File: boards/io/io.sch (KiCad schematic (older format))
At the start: 98 parts, among them J1 CU, J2 KB_ROW, J3 KB_COL, U1 74ACT32, U2 74ACT08, U3 74ACT00, U4 AT28C256-PLCC32, U5 62256-TSOP, U6 RC1602A, U7 74AC273, U8 74ACT244

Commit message: Part names
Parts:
- J1: value CU -> 61304021021
- R1: value 1 -> 0
- RV1: value 10-20k -> BOURNS 3296Y-1-203LF
- U1: value 74ACT32 -> SN74ACT32PWR
- U2: value 74ACT08 -> SN74ACT08PWR
- U3: value 74ACT00 -> 74ACT00MTCX
- U5: value 62256-TSOP -> CY62256NLL-55ZXI
- U6: value RC1602A -> SSW-116-01-T-S
- U7: value 74AC273 -> MC74AC273DTR2G
- U8: value 74ACT244 -> SN74ACT244PW
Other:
- moved on the sheet: C3, U2E, U3E
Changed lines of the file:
@@
 P 7550 2150
 F 0 "U5" H 8100 1200 50  0000 C CNN
-F 1 "62256-TSOP" H 7950 1050 50  0000 C CNN
+F 1 "CY62256NLL-55ZXI" H 7950 1050 50  0000 C CNN
 F 2 "Package_SO:TSOP-I-28_11.8x8mm_P0.55mm" H 7550 3000 50  0001 C CNN
 F 3 "http://www.farnell.com/datasheets/1674430.pdf" H 7550 3000 50  0001 C CNN
@@
 AR Path="/5E594F4F" Ref="U6"  Part="1"
 F 0 "U6" H 10650 1350 50  0000 C CNN
-F 1 "RC1602A" H 10850 1500 50  0000 C CNN
+F 1 "SSW-116-01-T-S" H 10850 1500 50  0000 C CNN
 F 2 "Connector_PinSocket_2.54mm:PinSocket_1x16_P2.54mm_Vertical" H 10450 1250 50  0001 C CNN
 F 3 "http://www.raystar-optronics.com/down.php?ProID=18" H 10450 1950 50  0001 C CNN
@@
 P 4850 4150
 F 0 "U2" H 4850 4475 50  0000 C CNN
-F 1 "74ACT08" H 4850 4384 50  0000 C CNN
+F 1 "SN74ACT08PWR" H 4850 4384 50  0000 C CNN
 F 2 "Package_SO:TSSOP-14_4.4x5mm_P0.65mm" H 4850 4150 50  0001 C CNN
 F 3 "http://www.ti.com/lit/gpn/sn74LS08" H 4850 4150 50  0001 C CNN
@@
 P 4850 4750
 F 0 "U2" H 4850 5075 50  0000 C CNN
-F 1 "74ACT08" H 4850 4984 50  0000 C CNN
+F 1 "SN74ACT08PWR" H 4850 4984 50  0000 C CNN
 F 2 "Package_SO:TSSOP-14_4.4x5mm_P0.65mm" H 4850 4750 50  0001 C CNN
 F 3 "http://www.ti.com/lit/gpn/sn74LS08" H 4850 4750 50  0001 C CNN
@@
 P 4300 6500
 F 0 "U2" H 4300 6825 50  0000 C CNN
-F 1 "74ACT08" H 4300 6734 50  0000 C CNN
+F 1 "SN74ACT08PWR" H 4300 6734 50  0000 C CNN
 F 2 "Package_SO:TSSOP-14_4.4x5mm_P0.65mm" H 4300 6500 50  0001 C CNN
 F 3 "http://www.ti.com/lit/gpn/sn74LS08" H 4300 6500 50  0001 C CNN
@@
 P 9000 4550
 F 0 "U2" H 9000 4875 50  0000 C CNN
-F 1 "74ACT08" H 9000 4784 50  0000 C CNN
+F 1 "SN74ACT08PWR" H 9000 4784 50  0000 C CNN
 F 2 "Package_SO:TSSOP-14_4.4x5mm_P0.65mm" H 9000 4550 50  0001 C CNN
 F 3 "http://www.ti.com/lit/gpn/sn74LS08" H 9000 4550 50  0001 C CNN
@@
 P 5550 4450
 F 0 "U3" H 5550 4775 50  0000 C CNN
-F 1 "74ACT00" H 5550 4684 50  0000 C CNN
+F 1 "74ACT00MTCX" H 5550 4684 50  0000 C CNN
 F 2 "Package_SO:TSSOP-14_4.4x5mm_P0.65mm" H 5550 4450 50  0001 C CNN
 F 3 "http://www.ti.com/lit/gpn/sn74hc00" H 5550 4450 50  0001 C CNN
@@
 P 6150 4700
 F 0 "U3" H 6150 5025 50  0000 C CNN
-F 1 "74ACT00" H 6150 4934 50  0000 C CNN
+F 1 "74ACT00MTCX" H 6150 4934 50  0000 C CNN
 F 2 "Package_SO:TSSOP-14_4.4x5mm_P0.65mm" H 6150 4700 50  0001 C CNN
 F 3 "http://www.ti.com/lit/gpn/sn74hc00" H 6150 4700 50  0001 C CNN
@@
 P 8400 4250
 F 0 "U3" H 8400 4575 50  0000 C CNN
-F 1 "74ACT00" H 8400 4484 50  0000 C CNN
+F 1 "74ACT00MTCX" H 8400 4484 50  0000 C CNN
 F 2 "Package_SO:TSSOP-14_4.4x5mm_P0.65mm" H 8400 4250 50  0001 C CNN
 F 3 "http://www.ti.com/lit/gpn/sn74hc00" H 8400 4250 50  0001 C CNN
@@
 P 7600 4250
 F 0 "U1" H 7600 4575 50  0000 C CNN
-F 1 "74ACT32" H 7600 4484 50  0000 C CNN
+F 1 "SN74ACT32PWR" H 7600 4484 50  0000 C CNN
 F 2 "Package_SO:TSSOP-14_4.4x5mm_P0.65mm" H 7600 4250 50  0001 C CNN
 F 3 "http://www.ti.com/lit/gpn/sn74LS32" H 7600 4250 50  0001 C CNN
@@
 P 6250 5600
 F 0 "U1" H 6250 5925 50  0000 C CNN
-F 1 "74ACT32" H 6250 5834 50  0000 C CNN
+F 1 "SN74ACT32PWR" H 6250 5834 50  0000 C CNN
 F 2 "Package_SO:TSSOP-14_4.4x5mm_P0.65mm" H 6250 5600 50  0001 C CNN
 F 3 "http://www.ti.com/lit/gpn/sn74LS32" H 6250 5600 50  0001 C CNN
@@
 P 3450 9150
 F 0 "U1" H 3680 9196 50  0000 L CNN
-F 1 "74ACT32" H 3680 9105 50  0000 L CNN
+F 1 "SN74ACT32PWR" H 3680 9105 50  0000 L CNN
 F 2 "Package_SO:TSSOP-14_4.4x5mm_P0.65mm" H 3450 9150 50  0001 C CNN
 F 3 "http://www.ti.com/lit/gpn/sn74LS32" H 3450 9150 50  0001 C CNN
@@
 L 74xx:74HC00 U3
 U 5 1 5E65CA62
-P 4400 9150
-F 0 "U3" H 4630 9196 50  0000 L CNN
-F 1 "74ACT00" H 4630 9105 50  0000 L CNN
-F 2 "Package_SO:TSSOP-14_4.4x5mm_P0.65mm" H 4400 9150 50  0001 C CNN
-F 3 "http://www.ti.com/lit/gpn/sn74hc00" H 4400 9150 50  0001 C CNN
-	5    4400 9150
+P 4550 9150
+F 0 "U3" H 4780 9196 50  0000 L CNN
+F 1 "74ACT00MTCX" H 4780 9105 50  0000 L CNN
+F 2 "Package_SO:TSSOP-14_4.4x5mm_P0.65mm" H 4550 9150 50  0001 C CNN
+F 3 "http://www.ti.com/lit/gpn/sn74hc00" H 4550 9150 50  0001 C CNN
+	5    4550 9150
 	1    0    0    -1
 $EndComp
@@
 L 74xx:74LS08 U2
 U 5 1 5E65F2AF
-P 5250 9150
-F 0 "U2" H 5480 9196 50  0000 L CNN
-F 1 "74ACT08" H 5480 9105 50  0000 L CNN
-F 2 "Package_SO:TSSOP-14_4.4x5mm_P0.65mm" H 5250 9150 50  0001 C CNN
-F 3 "http://www.ti.com/lit/gpn/sn74LS08" H 5250 9150 50  0001 C CNN
-	5    5250 9150
+P 5650 9150
+F 0 "U2" H 5880 9196 50  0000 L CNN
+F 1 "SN74ACT08PWR" H 5880 9105 50  0000 L CNN
+F 2 "Package_SO:TSSOP-14_4.4x5mm_P0.65mm" H 5650 9150 50  0001 C CNN
+F 3 "http://www.ti.com/lit/gpn/sn74LS08" H 5650 9150 50  0001 C CNN
+	5    5650 9150
 	1    0    0    -1
 $EndComp
@@
 P 10550 4700
 F 0 "U7" H 10950 4150 50  0000 C CNN
-F 1 "74AC273" H 10950 4000 50  0000 C CNN
+F 1 "MC74AC273DTR2G" H 10950 4000 50  0000 C CNN
 F 2 "Package_SO:TSSOP-20_4.4x6.5mm_P0.65mm" H 10550 4700 50  0001 C CNN
 F 3 "https://assets.nexperia.com/documents/data-sheet/74HC_HCT273.pdf" H 10550 4700 50  0001 C CNN
@@
 P 14250 4700
 F 0 "U8" H 14650 4150 50  0000 C CNN
-F 1 "74ACT244" H 14600 4000 50  0000 C CNN
+F 1 "SN74ACT244PW" H 14600 4000 50  0000 C CNN
 F 2 "Package_SO:TSSOP-20_4.4x6.5mm_P0.65mm" H 14250 4700 50  0001 C CNN
 F 3 "https://assets.nexperia.com/documents/data-sheet/74HC_HCT244.pdf" H 14250 4700 50  0001 C CNN
@@
 P 7650 5300
 F 0 "U1" H 7650 5625 50  0000 C CNN
-F 1 "74ACT32" H 7650 5534 50  0000 C CNN
+F 1 "SN74ACT32PWR" H 7650 5534 50  0000 C CNN
 F 2 "Package_SO:TSSOP-14_4.4x5mm_P0.65mm" H 7650 5300 50  0001 C CNN
 F 3 "http://www.ti.com/lit/gpn/sn74LS32" H 7650 5300 50  0001 C CNN
@@
 P 7650 5850
 F 0 "U1" H 7650 6175 50  0000 C CNN
-F 1 "74ACT32" H 7650 6084 50  0000 C CNN
+F 1 "SN74ACT32PWR" H 7650 6084 50  0000 C CNN
 F 2 "Package_SO:TSSOP-14_4.4x5mm_P0.65mm" H 7650 5850 50  0001 C CNN
 F 3 "http://www.ti.com/lit/gpn/sn74LS32" H 7650 5850 50  0001 C CNN
@@
 P 4300 7050
 F 0 "U3" H 4300 7375 50  0000 C CNN
-F 1 "74ACT00" H 4300 7284 50  0000 C CNN
+F 1 "74ACT00MTCX" H 4300 7284 50  0000 C CNN
 F 2 "Package_SO:TSSOP-14_4.4x5mm_P0.65mm" H 4300 7050 50  0001 C CNN
 F 3 "http://www.ti.com/lit/gpn/sn74hc00" H 4300 7050 50  0001 C CNN
@@
 P 11300 1850
 F 0 "RV1" H 11230 1804 50  0000 R CNN
-F 1 "10-20k" H 11230 1895 50  0000 R CNN
+F 1 "BOURNS 3296Y-1-203LF" H 11230 1895 50  0000 R CNN
 F 2 "Potentiometer_THT:Potentiometer_Bourns_3296Z_Horizontal" H 11300 1850 50  0001 C CNN
 F 3 "~" H 11300 1850 50  0001 C CNN
@@
 P 11100 2350
 F 0 "R1" V 11200 2350 50  0000 C CNN
-F 1 "1" V 11000 2350 50  0000 C CNN
+F 1 "0" V 11000 2350 50  0000 C CNN
 F 2 "Resistor_SMD:R_0805_2012Metric" V 11030 2350 50  0001 C CNN
 F 3 "~" H 11100 2350 50  0001 C CNN
@@
 AR Path="/5E72DAA8" Ref="J1"  Part="1"
 F 0 "J1" H 1800 4217 50  0000 C CNN
-F 1 "CU" H 1800 4126 50  0000 C CNN
+F 1 "61304021021" H 1800 4126 50  0000 C CNN
 F 2 "Connector_PinHeader_2.54mm:PinHeader_2x20_P2.54mm_Horizontal" H 1750 3100 50  0001 C CNN
 F 3 "~" H 1750 3100 50  0001 C CNN
@@
 L power:GND #PWR0102
 U 1 1 5E7372E2
-P 4400 9650
-F 0 "#PWR0102" H 4400 9400 50  0001 C CNN
-F 1 "GND" H 4405 9477 50  0000 C CNN
-F 2 "" H 4400 9650 50  0001 C CNN
-F 3 "" H 4400 9650 50  0001 C CNN
-	1    4400 9650
+P 4550 9650
+F 0 "#PWR0102" H 4550 9400 50  0001 C CNN
+F 1 "GND" H 4555 9477 50  0000 C CNN
+F 2 "" H 4550 9650 50  0001 C CNN
+F 3 "" H 4550 9650 50  0001 C CNN
+	1    4550 9650
 	1    0    0    -1
 $EndComp
@@
 L power:GND #PWR0103
 U 1 1 5E7377AC
-P 5250 9650
-F 0 "#PWR0103" H 5250 9400 50  0001 C CNN
-F 1 "GND" H 5255 9477 50  0000 C CNN
-F 2 "" H 5250 9650 50  0001 C CNN
-F 3 "" H 5250 9650 50  0001 C CNN
-	1    5250 9650
+P 5650 9650
+F 0 "#PWR0103" H 5650 9400 50  0001 C CNN
+F 1 "GND" H 5655 9477 50  0000 C CNN
+F 2 "" H 5650 9650 50  0001 C CNN
+F 3 "" H 5650 9650 50  0001 C CNN
+	1    5650 9650
 	1    0    0    -1
 $EndComp
@@
 L power:VCC #PWR0105
 U 1 1 5E738B21
-P 4400 8650
-F 0 "#PWR0105" H 4400 8500 50  0001 C CNN
-F 1 "VCC" H 4417 8823 50  0000 C CNN
-F 2 "" H 4400 8650 50  0001 C CNN
-F 3 "" H 4400 8650 50  0001 C CNN
-	1    4400 8650
+P 4550 8650
+F 0 "#PWR0105" H 4550 8500 50  0001 C CNN
+F 1 "VCC" H 4567 8823 50  0000 C CNN
+F 2 "" H 4550 8650 50  0001 C CNN
+F 3 "" H 4550 8650 50  0001 C CNN
+	1    4550 8650
 	1    0    0    -1
 $EndComp
@@
 L power:VCC #PWR0106
 U 1 1 5E739058
-P 5250 8650
-F 0 "#PWR0106" H 5250 8500 50  0001 C CNN
-F 1 "VCC" H 5267 8823 50  0000 C CNN
-F 2 "" H 5250 8650 50  0001 C CNN
-F 3 "" H 5250 8650 50  0001 C CNN
-	1    5250 8650
+P 5650 8650
+F 0 "#PWR0106" H 5650 8500 50  0001 C CNN
+F 1 "VCC" H 5667 8823 50  0000 C CNN
+F 2 "" H 5650 8650 50  0001 C CNN
+F 3 "" H 5650 8650 50  0001 C CNN
+	1    5650 8650
 	1    0    0    -1
 $EndComp
@@
 L Device:C C3
 U 1 1 5E762C60
-P 6100 9150
-F 0 "C3" H 6215 9196 50  0000 L CNN
-F 1 "0.1u" H 6215 9105 50  0000 L CNN
-F 2 "Capacitor_SMD:C_0805_2012Metric" H 6138 9000 50  0001 C CNN
-F 3 "~" H 6100 9150 50  0001 C CNN
-	1    6100 9150
+P 6500 9150
+F 0 "C3" H 6615 9196 50  0000 L CNN
+F 1 "0.1u" H 6615 9105 50  0000 L CNN
+F 2 "Capacitor_SMD:C_0805_2012Metric" H 6538 9000 50  0001 C CNN
+F 3 "~" H 6500 9150 50  0001 C CNN
+	1    6500 9150
 	1    0    0    -1
 $EndComp
@@
 L power:GND #PWR034
 U 1 1 5E762C66
-P 6100 9300
-F 0 "#PWR034" H 6100 9050 50  0001 C CNN
-F 1 "GND" H 6105 9127 50  0000 C CNN
-F 2 "" H 6100 9300 50  0001 C CNN
-F 3 "" H 6100 9300 50  0001 C CNN
-	1    6100 9300
+P 6500 9300
+F 0 "#PWR034" H 6500 9050 50  0001 C CNN
+F 1 "GND" H 6505 9127 50  0000 C CNN
+F 2 "" H 6500 9300 50  0001 C CNN
+F 3 "" H 6500 9300 50  0001 C CNN
+	1    6500 9300
 	1    0    0    -1
 $EndComp
@@
 L power:VCC #PWR033
 U 1 1 5E762C6C
-P 6100 9000
-F 0 "#PWR033" H 6100 8850 50  0001 C CNN
-F 1 "VCC" H 6117 9173 50  0000 C CNN
-F 2 "" H 6100 9000 50  0001 C CNN
-F 3 "" H 6100 9000 50  0001 C CNN
-	1    6100 9000
-	1    0    0    -1
-$EndComp
+P 6500 9000
+F 0 "#PWR033" H 6500 8850 50  0001 C CNN
+F 1 "VCC" H 6517 9173 50  0000 C CNN
+F 2 "" H 6500 9000 50  0001 C CNN
+F 3 "" H 6500 9000 50  0001 C CNN
+	1    6500 9000
+	1    0    0    -1
+$EndComp

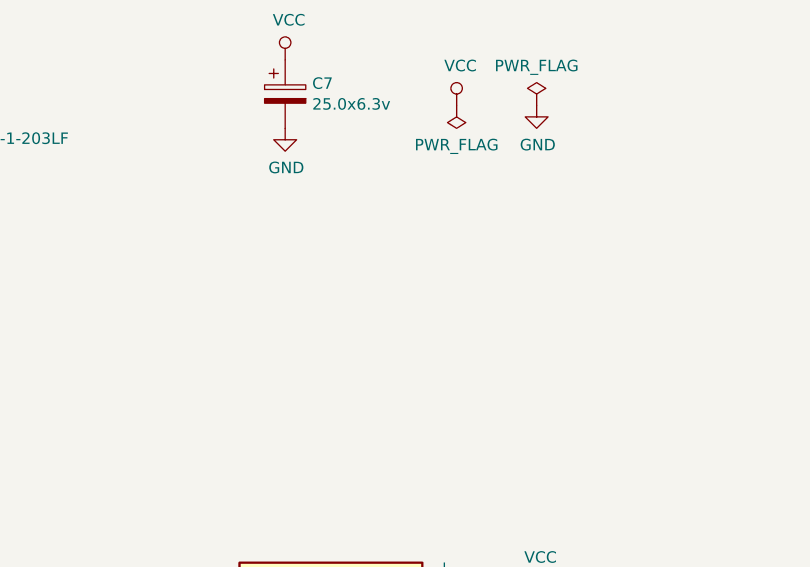
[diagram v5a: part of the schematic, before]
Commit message: Power connector on the IO board
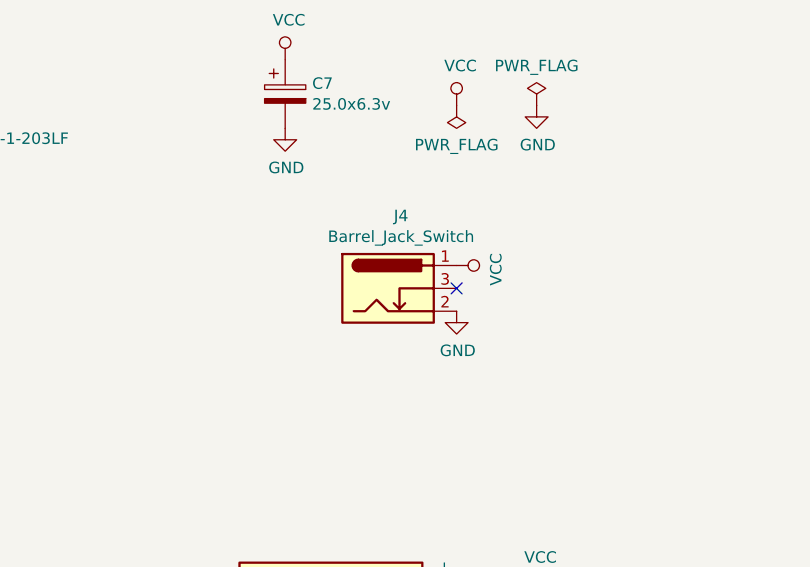
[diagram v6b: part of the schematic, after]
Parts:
- added J4: Barrel_Jack_Switch, Connector_BarrelJack:BarrelJack_Wuerth_6941xx301002, symbol Connector:Barrel_Jack_Switch
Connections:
- net GND: now also J4.2
- net VCC: now also J4.1
- no-connect marks 11 -> 12
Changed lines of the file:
@@
 	1    0    0    -1
 $EndComp
+$Comp
+L Connector:Barrel_Jack_Switch J4
+U 1 1 5ED6F149
+P 13600 2550
+F 0 "J4" H 13657 2867 50  0000 C CNN
+F 1 "Barrel_Jack_Switch" H 13657 2776 50  0000 C CNN
+F 2 "Connector_BarrelJack:BarrelJack_Wuerth_6941xx301002" H 13650 2510 50  0001 C CNN
+F 3 "~" H 13650 2510 50  0001 C CNN
+	1    13600 2550
+	1    0    0    -1
+$EndComp
+$Comp
+L power:GND #PWR0108
+U 1 1 5ED703DB
+P 13900 2650
+F 0 "#PWR0108" H 13900 2400 50  0001 C CNN
+F 1 "GND" H 13905 2477 50  0000 C CNN
+F 2 "" H 13900 2650 50  0001 C CNN
+F 3 "" H 13900 2650 50  0001 C CNN
+	1    13900 2650
+	1    0    0    -1
+$EndComp
+$Comp
+L power:VCC #PWR0109
+U 1 1 5ED707C6
+P 13900 2450
+F 0 "#PWR0109" H 13900 2300 50  0001 C CNN
+F 1 "VCC" H 13917 2623 50  0000 C CNN
+F 2 "" H 13900 2450 50  0001 C CNN
+F 3 "" H 13900 2450 50  0001 C CNN
+	1    13900 2450
+	0    1    1    0
+$EndComp
+NoConn ~ 13900 2550
 Wire Bus Line
 	15050 4100 15050 5000

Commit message: New IO board model and schematic diagram
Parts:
- removed J2: KB_ROW, Connector_PinHeader_2.54mm:PinHeader_1x08_P2.54mm_Vertical, symbol Connector_Generic:Conn_01x08
- removed J3: KB_COL, Connector_PinHeader_2.54mm:PinHeader_1x08_P2.54mm_Vertical, symbol Connector_Generic:Conn_01x08
- removed R1: 0, Resistor_SMD:R_0805_2012Metric, symbol Device:R
- removed U2: SN74ACT08PWR, Package_SO:TSSOP-14_4.4x5mm_P0.65mm, symbol 74xx:74LS08
- added C8, C9, C? (x4): 0.1u, Capacitor_SMD:C_0805_2012Metric, symbol Device:C
- added D? (x8): KP-2012EC, LED_SMD:LED_0805_2012Metric, symbol Device:LED
- added J2, J6: SSW-120-02-G-D-RA, Connector_PinHeader_2.54mm:PinHeader_2x20_P2.54mm_Horizontal, symbol Connector_Generic:Conn_02x20_Odd_Even
- added J3, J5: Conn_01x09, symbol Connector_Generic:Conn_01x09
- added Q1: Q_NMOS_DGS, symbol Device:Q_NMOS_DGS
- added R? (x8): 620, Resistor_SMD:R_0805_2012Metric, symbol Device:R
- added U10: 74HC151, symbol 74xx:74LS151
- added U11: MC74AC273DTR2G, Package_SO:TSSOP-20_4.4x6.5mm_P0.65mm, symbol 74xx:74HC273
- added U12, U14: 74LS32, symbol 74xx:74LS32
- added U13: CY62256NLL-55ZXI, Package_SO:TSOP-I-28_11.8x8mm_P0.55mm, symbol missing:62256-TSOP
- added U2, U9: 74LS30, symbol 74xx:74LS30
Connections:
- net GND: now also C8.2, C9.2, C?.2, C?.2, C?.2, C?.2, J2.2 (Pin_2), J2.39 (Pin_39), J3.9 (Pin_9), J6.2 (Pin_2), J6.39 (Pin_39), Q1.3 (S), R?.1, R?.1, R?.1, R?.1, R?.1, R?.1, R?.1, R?.1, U10.12 (I7), U10.8 (GND), U11.10 (GND), U12.7 (GND), U13.21 (GND), U14.12, U14.13, U14.7 (GND), U2.7 (GND), U9.7 (GND); no longer J1.5 (Pin_5)
- net VCC: now also U6.15 (A/VEE), C8.1, C9.1, C?.1, C?.1, C?.1, C?.1, J2.1 (Pin_1), J2.40 (Pin_40), J5.9 (Pin_9), J6.1 (Pin_1), J6.40 (Pin_40), U10.16 (VCC), U10.3 (I1), U10.4 (I0), U11.20 (VCC), U12.14 (VCC), U13.7 (VCC), U14.14 (VCC), U2.1, U2.11, U2.12, U2.14 (VCC), U2.2, U9.14 (VCC); no longer U7.1 (~Mr)
- net a0: now also J2.23 (Pin_23), J6.23 (Pin_23), U13.17 (A0)
- net a1: now also U1.2, J2.24 (Pin_24), J6.24 (Pin_24), U12.12, U13.16 (A1); no longer U1.5
- net a10: now also J2.33 (Pin_33), J6.33 (Pin_33), U13.28 (A10), U9.3
- net a11: now also J2.34 (Pin_34), J6.34 (Pin_34), U13.2 (A11), U9.4
- net a12: now also J2.35 (Pin_35), J6.35 (Pin_35), U10.11 (S0), U13.9 (A12), U9.5
- net a13: now also J2.36 (Pin_36), J6.36 (Pin_36), U10.10 (S1), U13.5 (A13), U9.6
- net a14: now also J2.37 (Pin_37), J6.37 (Pin_37), U10.9 (S2), U13.8 (A14), U9.11
- net a15: now also U3.1, U3.2, J2.38 (Pin_38), J6.38 (Pin_38), U12.1, U9.12; no longer U3.5, U4.23 (~CE)
- net a2: now also U1.1, J2.25 (Pin_25), J6.25 (Pin_25), U13.15 (A2), U14.2
- net a3: now also J2.26 (Pin_26), J6.26 (Pin_26), U13.14 (A3)
- net a4: now also J2.27 (Pin_27), J6.27 (Pin_27), U13.13 (A4)
- net a5: now also J2.28 (Pin_28), J6.28 (Pin_28), U13.12 (A5)
- net a6: now also J2.29 (Pin_29), J6.29 (Pin_29), U13.11 (A6)
- net a7: now also J2.30 (Pin_30), J6.30 (Pin_30), U13.10 (A7)
- net a8: now also J2.31 (Pin_31), J6.31 (Pin_31), U13.4 (A8), U9.1
- net a9: now also J2.32 (Pin_32), J6.32 (Pin_32), U13.3 (A9), U9.2
- net d0: now also J2.11 (Pin_11), J6.11 (Pin_11), U11.3 (D0), U13.18 (D0)
- net d1: now also J2.12 (Pin_12), J6.12 (Pin_12), U11.4 (D1), U13.19 (D1)
- net d2: now also J2.13 (Pin_13), J6.13 (Pin_13), U11.7 (D2), U13.20 (D2)
- net d3: now also J2.14 (Pin_14), J6.14 (Pin_14), U11.8 (D3), U13.22 (D3)
- net d4: now also J2.15 (Pin_15), J6.15 (Pin_15), U11.13 (D4), U13.23 (D4)
- net d5: now also J2.16 (Pin_16), J6.16 (Pin_16), U11.14 (D5), U13.24 (D5)
- net d6: now also J2.17 (Pin_17), J6.17 (Pin_17), U11.17 (D6), U13.25 (D6)
- net d7: now also J2.18 (Pin_18), J6.18 (Pin_18), U11.18 (D7), U13.26 (D7)
- net lcd_e: now also U3.8
- net ~io_cs: now also U1.5, U12.9, U14.9, U2.6, U9.8; no longer U1.2, U1.4, U3.3, U3.4
- net ~oe: now also J2.7 (Pin_7), J6.7 (Pin_7), U13.1 (~OE)
- net ~ram_cs: no longer U3.6, U5.27 (~CS)
- net ~rst: now also U7.1 (~Mr), J2.4 (Pin_4), J6.4 (Pin_4), U11.1 (~Mr)
- net ~we: now also J2.8 (Pin_8), J6.8 (Pin_8), U12.4, U13.6 (~WE), U14.10; no longer U1.1
- net ~lcd_e: now reaches U3.10, U3.9
- net ~lcd_e: now also U14.6; no longer U1.3
- net at R46.1, U8.11 (2A3): now also J5.1 (Pin_1)
- net at R45.1, U8.13 (2A2): now also J5.2 (Pin_2)
- net at R44.1, U8.15 (2A1): now also J5.3 (Pin_3)
- net at R43.1, U8.17 (2A0): now also J5.4 (Pin_4)
- net at R39.1, U8.2 (1A0): now also J5.8 (Pin_8)
- net at R40.1, U8.4 (1A1): now also J5.7 (Pin_7)
- net at R41.1, U8.6 (1A2): now also J5.6 (Pin_6)
- net at R42.1, U8.8 (1A3): now also J5.5 (Pin_5)
- net at R7.1: now also J3.1 (Pin_1)
- net at R8.1: now also J3.2 (Pin_2)
- net at R9.1: now also J3.3 (Pin_3)
- net at R10.1: now also J3.4 (Pin_4)
- net at R11.1: now also J3.5 (Pin_5)
- net at R12.1: now also J3.6 (Pin_6)
- net at R13.1: now also J3.7 (Pin_7)
- net at R14.1: now also J3.8 (Pin_8)
- new net: U1.3, U1.4
- new net: U12.10, U12.11
- new net: U14.3, U14.4
- new net: U14.5, U14.8
- new net: Q1.2 (G), U2.8
- new net: D?.1 (K), R?.2 (x8)
- new net cr_cp: U11.11 (Cp), U12.6
- new net l_ena: D?.2 (A), J2.6 (Pin_6), U11.5 (Q1)
- new net r_ena: D?.2 (A), J6.6 (Pin_6), U11.6 (Q2)
- new net ram_a_ena: D?.2 (A), U10.2 (I2), U11.9 (Q3)
- new net ram_b_ena: D?.2 (A), U10.1 (I3), U11.12 (Q4)
- new net ram_c_ena: D?.2 (A), U10.15 (I4), U11.15 (Q5)
- new net ram_d_ena: D?.2 (A), U10.14 (I5), U11.16 (Q6)
- new net ram_e_ena: D?.2 (A), U10.13 (I6), U11.19 (Q7)
- new net raml_ena: D?.2 (A), U11.2 (Q0), U12.2, U3.5
- new net ~a1: U14.1
- new net ~a15: U10.7 (~E), U3.3, U3.4
- new net ~a2: U12.13
- new net ~cr_cs: U12.5, U12.8
- new net ~ramh_cs: U10.6 (~Z), U2.5, U5.27 (~CS)
- new net ~raml_cs: U13.27 (~CS), U2.4, U3.6
- new net ~rdy: J1.5 (Pin_5), J2.5 (Pin_5), J6.5 (Pin_5), Q1.1 (D)
- new net ~rom_cs: U12.3, U2.3, U4.23 (~CE)
- no-connect marks 12 -> 27
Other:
- note added: "0000-7FFF ROM or RAM (selected by raml_ena in CR)\n8000-EFFF RAM\nF000-FEFF empty\nFF00-FFFF IO\n"
- note added: "FF00 Keyboard\nFF02 LCD control\nFF03 LCD data\nFF04 Control register"
- note added: "See model/io.v and model/test/test_io.v"
- note removed: "0000-7FFF ROM\n8000-EFFF RAM\nF000-FFFF IO\n"
- note removed: "F000 Keyboard\nF002 LCD control\nF003 LCD data"
- moved on the sheet: C1, C3, C5, C6, C7, D1, D10, D11, D12, D13, D14, D15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
